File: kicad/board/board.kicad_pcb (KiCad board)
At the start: 2 copper layers, 110 x 70 mm, 72 parts, among them J0 Netz

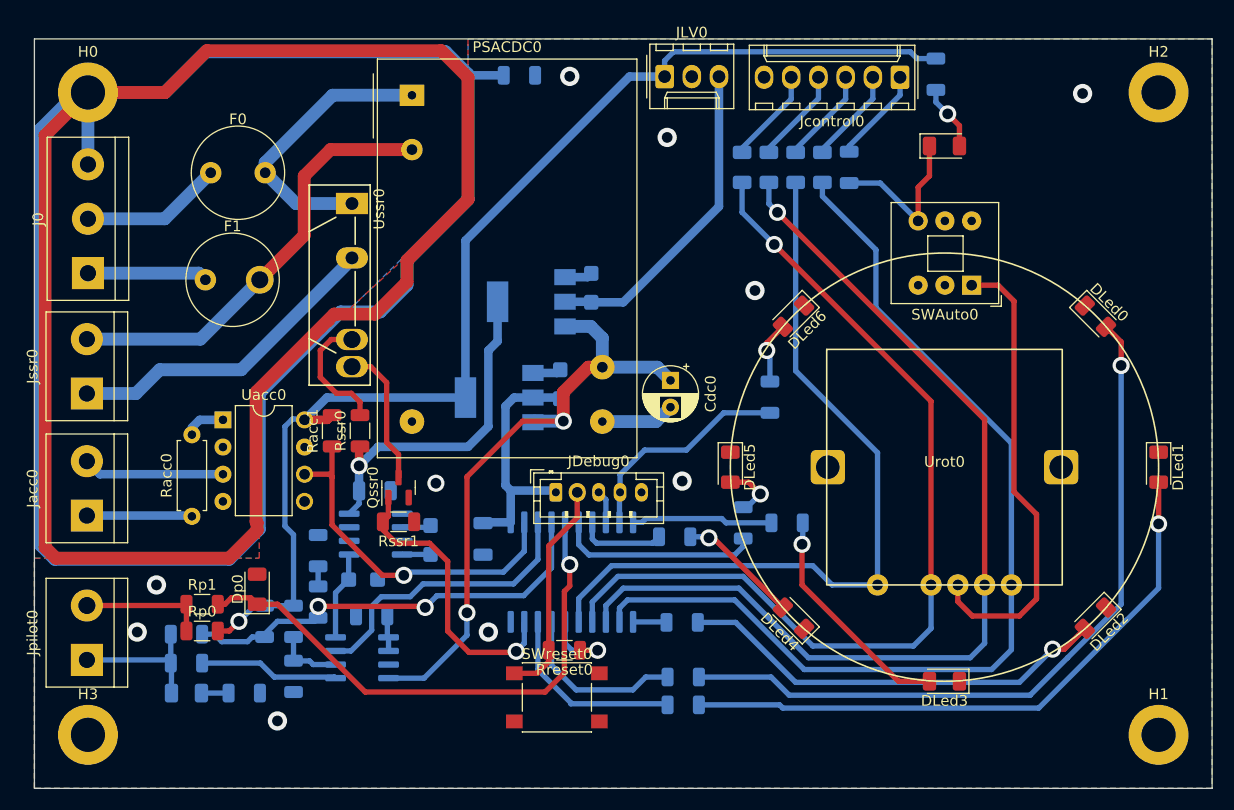
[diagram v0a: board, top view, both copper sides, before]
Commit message: hardware: kicad board bestellt
simplifiziert:
Strom sowie Fehlerstrom werden durch Hauptsicherung und FI gesichert.
AC-Check is a recht sinnlos weil gegen ein hängendes Relais kannst
eh nit viel tun.
Diodencheck macht sinn, wird auch mit -5V statt den Spezifizierten -12V
duchgeführt, sollt genauso funktionieren, meine LTC1044 halten max 9V aus.
Rechtck-Puls wird mit Transistor-Brücke realisiert (simuliert, nicht
getestet). Steigende Flanke wird begrenzt durch pull-down Widerstand
(auf -5V) und parasitic capazity.
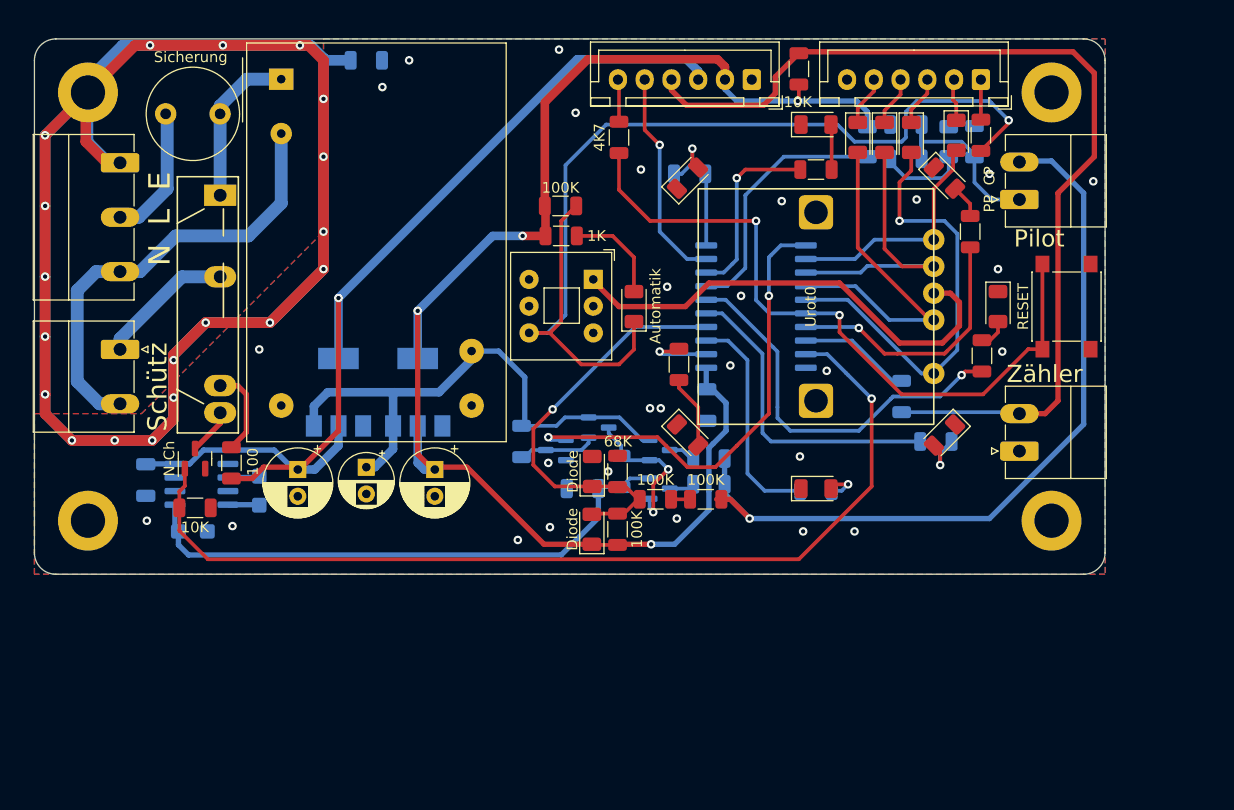
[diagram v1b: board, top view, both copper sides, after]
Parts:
- removed F1: 100m, Fuse:Fuse_Littelfuse_372_D8.50mm
- removed JDebug0: Conn_01x05, Connector_JST:JST_PH_B5B-PH-K_1x05_P2.00mm_Vertical
- removed JLV0: Conn_01x03, Connector_Molex:Molex_KK-254_AE-6410-03A_1x03_P2.54mm_Vertical
- removed Jacc0: AC-Control, TerminalBlock:TerminalBlock_bornier-2_P5.08mm
- removed Jpilot0: PILOT, TerminalBlock:TerminalBlock_bornier-2_P5.08mm
- removed Jssr0: Schütz, TerminalBlock:TerminalBlock_bornier-2_P5.08mm
- removed Racc0: 22K, Resistor_THT:R_Axial_DIN0207_L6.3mm_D2.5mm_P7.62mm_Horizontal
- removed Racc1, Rp1, Rpc0, Rpc8: 10K, Resistor_SMD:R_1206_3216Metric
- removed Rpc3: 1K, Resistor_SMD:R_1206_3216Metric
- removed Rpc6: 3K3, Resistor_SMD:R_1206_3216Metric
- removed Uacc0: MID400, Package_DIP:DIP-8_W7.62mm
- removed Upc0: LM358, Package_SO:SOIC-8_3.9x4.9mm_P1.27mm
- added (1K5): 1K5, Resistor_SMD:R_1206_3216Metric, B.Cu at (137.8, 59.6)
- added 100K: 100K, Resistor_SMD:R_1206_3216Metric, F.Cu at (99.1, 65.6)
- added 100K: 100K, Resistor_SMD:R_1206_3216Metric, F.Cu at (112.7, 93.0)
- added 10K: 10K, Resistor_SMD:R_1206_3216Metric, F.Cu at (121.4, 52.8)
- added 10K: 4K7, Resistor_SMD:R_1206_3216Metric, B.Cu at (131.4, 61.2)
- added 10K: 10k, Resistor_SMD:R_1206_3216Metric, B.Cu at (95.5, 87.6)
- added 10p: 10p, Capacitor_SMD:C_1206_3216Metric, B.Cu at (101.2, 92.0)
- added 1K: 1K, Resistor_SMD:R_1206_3216Metric, B.Cu at (113.0, 91.6)
- added 1K: 1K, Resistor_SMD:R_1206_3216Metric, B.Cu at (131.0, 83.4)
- added Diode: D, Diode_SMD:D_1206_3216Metric, F.Cu at (102.1, 95.8)
- added Diode: D, Diode_SMD:D_1206_3216Metric, B.Cu at (127.8, 59.6)
- added J1: Conn_01x02, Connector_Phoenix_MC:PhoenixContact_MC_1,5_2-G-3.5_1x02_P3.50mm_Horizontal, F.Cu at (142.0, 88.5)
- added J2: Schütz, Connector_Phoenix_MC_HighVoltage:PhoenixContact_MC_1,5_2-G-5.08_1x02_P5.08mm_Horizontal, F.Cu at (58.0, 79.0)
- added J3: Pilot, Connector_Phoenix_MC:PhoenixContact_MC_1,5_2-G-3.5_1x02_P3.50mm_Horizontal, F.Cu at (142.0, 65.0)
- added Jcontrol1: Conn_01x06, Connector_JST:JST_XH_B6B-XH-A_1x06_P2.50mm_Vertical, F.Cu at (117.0, 53.8)
- added N-Ch: MMBF170, Package_TO_SOT_SMD:SOT-23, B.Cu at (98.7, 88.4)
- added N-Ch: MMBF170, Package_TO_SOT_SMD:SOT-23, B.Cu at (108.4, 92.0)
- added P-Ch: IRLML5203, Package_TO_SOT_SMD:SOT-23, B.Cu at (108.4, 88.4)
- added P-Ch: IRLML5203, Package_TO_SOT_SMD:SOT-23, B.Cu at (102.7, 86.3)
- 100K: renamed from Rpc4; value 68K -> 100K; moved to F.Cu
- 100K: renamed from Rpc7; value 22K -> 100K; moved to F.Cu
- 1K: renamed from RAuto0; moved to F.Cu
- 3.3 V: renamed from Udc0
- 3K3: renamed from Rpc1; value 10K -> 3k3
- 3K3: renamed from Rp0; value 1K -> 3K3; moved to B.Cu
- 5 V: renamed from Udc1
- 68K: renamed from Rpc5; value 22K -> 68K; moved to F.Cu
- Cdc1, Cdc2: footprint Capacitor_Tantalum_SMD:CP_EIA-3216-12_Kemet-S -> Capacitor_THT:CP_Radial_D6.3mm_P2.50mm; moved to F.Cu
- Dc0, Dc1, Dc2, Dc3: moved to F.Cu
- Diode: renamed from Dpc0; moved to F.Cu
- Diode: renamed from Dp0; moved to B.Cu
- J0: footprint TerminalBlock:TerminalBlock_bornier-3_P5.08mm -> Connector_Phoenix_MC_HighVoltage:PhoenixContact_MC_1,5_3-G-5.08_1x03_P5.08mm_Horizontal
- Jcontrol0: footprint Connector_Molex:Molex_KK-254_AE-6410-06A_1x06_P2.54mm_Vertical -> Connector_JST:JST_XH_B6B-XH-A_1x06_P2.50mm_Vertical
- RAuto2: renamed from RAut1; moved to F.Cu
- RLed0, RLed4, RLed5: value 1K -> 470
- RLed1, RLed2, RLed3, RLed6: value 1K -> 470; moved to F.Cu
- moved 3K3 81.0 mm to (131.4, 58.0), turned to 180 degrees
- moved Diode 76.9 mm to (135.4, 59.6)
- moved RESET 60.0 mm to (146.4, 75.0), turned to 90 degrees
- moved 1K 52.4 mm to (113.0, 89.2)
- moved RLed1 51.5 mm to (123.0, 62.2)
- moved 4K7 48.2 mm to (104.6, 59.2), turned to 90 degrees
- moved RLed0 47.0 mm to (111.2, 62.6), turned to 180 degrees
- moved 100K 45.6 mm to (108.0, 93.0), turned to 0 degrees
- moved RLed2 45.3 mm to (137.4, 68.0), turned to 90 degrees
- moved DLed1 45.3 mm to (123.0, 58.0), turned to 0 degrees
- moved DLed2 43.5 mm to (135.0, 63.0), turned to -45 degrees
- moved Diode 43.2 mm to (102.1, 90.4), turned to 90 degrees
- moved DLed0 40.2 mm to (111.0, 63.0), turned to 45 degrees
- moved 1K 38.1 mm to (99.2, 68.4), turned to 180 degrees
- moved 3K3 36.1 mm to (104.8, 90.4)
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- renumbered Rgnd0 to 10, Rssr0 to 100, Rssr1 to 10K, Cndc0 to 10p, Cndc2 to 10u, Cndc1 to 10u, Rpc2 to 1K, Rreset0 to 4K7, Utiny0 to Attiny1616, Undc0 to LTC1044, DLed6 to Led6, Qssr0 to N-Ch, SWreset0 to RESET, F0 to Sicherung
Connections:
- 100K pad 2: Control Pilot -> Net-(Rpc4-Pad2)
- 1K pad 1: Net-(Upc0-Pad1) -> Control Pilot
- 1K pad 2: Control Pilot -> Net-(Q1-Pad3)
- 3K3 pad 2: GND -> -5V
- 68K pad 1: Net-(Rpc5-Pad1) -> GND
- Attiny1616 pad 10: Led3 -> Led0
- Attiny1616 pad 11: Led2 -> PWM
- Attiny1616 pad 17: Led0 -> Led2
- Attiny1616 pad 18: Led1 -> Stromzähler
- Attiny1616 pad 2: AC-Check -> Led6
- Attiny1616 pad 3: PWM -> Led5
- Attiny1616 pad 5: PP Read -> Led4
- Attiny1616 pad 6: Led5 -> Led3
- Attiny1616 pad 7: Led4 -> PP Read
- Attiny1616 pad 8: Uart_RX -> Led1
- Diode pad 1: Control Pilot -> CP-Read
- Diode pad 2: Net-(Rpc3-Pad2) -> GND
- J0 pad 1: /ACN -> Earth
- J0 pad 3: Earth -> VAC
- RESET pad 1: UPDI -> Net-(Rreset0-Pad1)
- RLed6 pad 1: Uart_TX -> Led6
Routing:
- net Zähler_ext: track 0.00 -> 92.1 mm
- net Auto: track 15.3 -> 96.5 mm, vias 0 -> 1
- net Earth: track 324.0 -> 246.0 mm, vias 0 -> 19
- net A: track 92.6 -> 21.9 mm
- net C: track 92.2 -> 26.5 mm, vias 1 -> 0
- net Net-(DLed0-Pad2): track 70.2 -> 5.46 mm
- net Relais: track 27.3 -> 90.7 mm
- net Control Pilot: track 13.5 -> 73.9 mm, vias 0 -> 1
- net Net-(Rreset0-Pad1): track 6.95 -> 65.9 mm, vias 1 -> 2
- net D: track 86.8 -> 32.1 mm, vias 1 -> 0
- net Net-(DLed1-Pad2): track 57.6 -> 4.23 mm, vias 1 -> 0
- net -5V: track 8.27 -> 52.8 mm
- net Net-(DLed2-Pad2): track 40.5 -> 3.13 mm, vias 1 -> 0
- net +5V: track 62.4 -> 97.1 mm
- net AC-Check: track 33.7 -> 0.00 mm, vias 1 -> 0
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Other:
- board size 110 x 70 mm -> 100 x 50 mm
- board text added: "+12V"
- board text added: "-5V"
- board text added: "Automatik"
- board text added: "Control Pilot"
- board text added: "E L N"
- board text added: "EVSE Wallbox Johnny Jan.2023"
- board text added: "N L E"
- board text added: "PP CP"
- board text added: "Pilot"
- board text added: "Prox. Pilot"
- board text added: "Relais"
- board text added: "Schütz"
- board text added: "UPDI TX Zähler 5V 3.3V GND"
- board text added: "X A B C D Gnd"
- board text added: "Zähler"

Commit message: hardware: korrekturen fehlerhaftes pcb
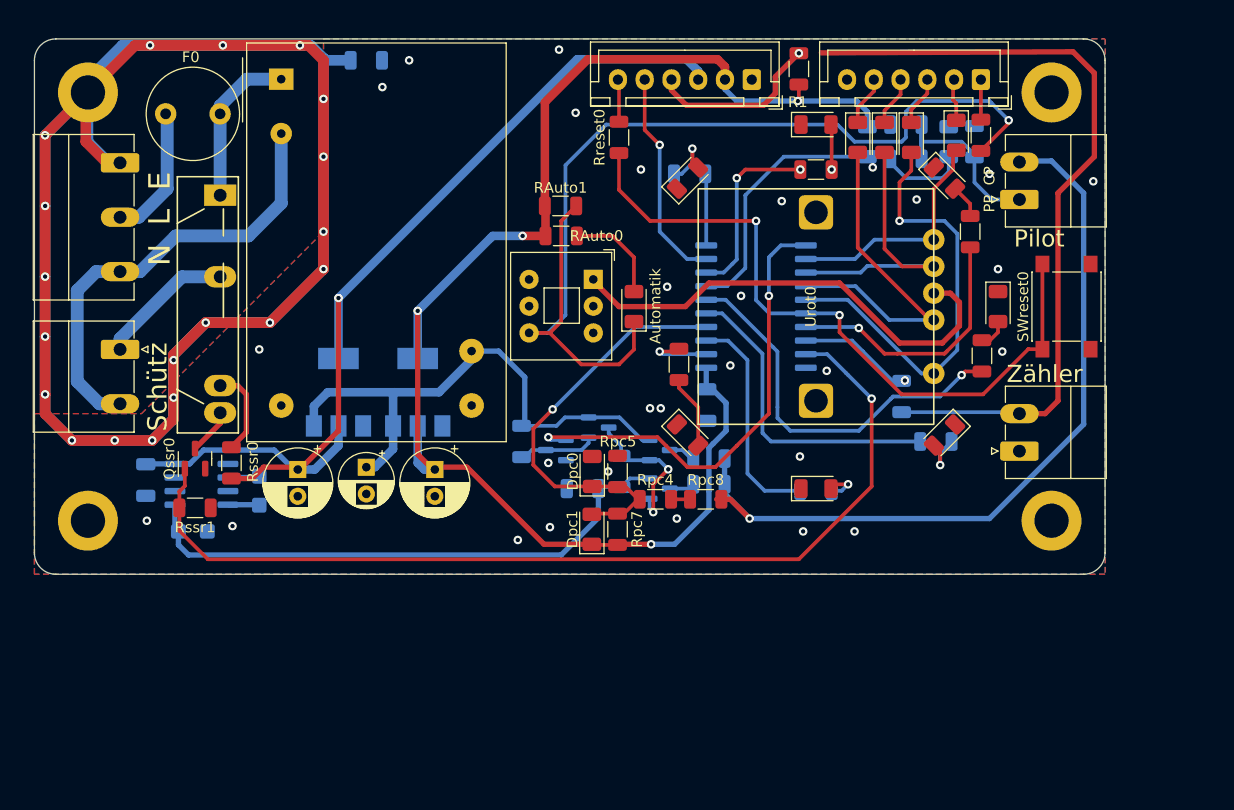
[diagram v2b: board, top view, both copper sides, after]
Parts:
- Udc0: renamed from 3.3 V
- Udc1: renamed from 5 V
- renumbered 10p to Cdpc1, 10p to Cndc0, 10u to Cndc1, 10u to Cndc2, Led6 to DLed6, Diode to Dp0, Diode to Dp1, Diode to Dpc0, Diode to Dpc1, Sicherung to F0, P-Ch to Q1, P-Ch to Q2, N-Ch to Qssr0, N-Ch to Qssr1, N-Ch to Qssr2, 10K to R1, 1K to R2, 1K to RAuto0, 100K to RAuto1, 10 to Rgnd0, 3K3 to Rp0, 10K to Rp1, 3K3 to Rpc1, 1K to Rpc2, 10K to Rpc3, 100K to Rpc4, 68K to Rpc5, 1K to Rpc6, 100K to Rpc7, 100K to Rpc8, (1K5) to Rpp0, 4K7 to Rreset0, 100 to Rssr0, 10K to Rssr1, RESET to SWreset0, LTC1044 to Undc0, Attiny1616 to Utiny0
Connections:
- DLed_auto0 pad 1: Auto -> PP Read
- J1 pad 2: Zähler_ext -> Net-(DLed1-Pad2)
- Jcontrol1 pad 4: Zähler_ext -> Uart_RX
- R1 pad 2: Zähler_ext -> Uart_RX
- R2 pad 1: Zähler_ext -> Net-(DLed1-Pad2)
- R2 pad 2: Stromzähler -> Led1
- RAuto1 pad 1: Auto -> PP Read
- RAuto2 pad 2: Auto -> PP Read
- RLed1 pad 1: Led1 -> Uart_RX
- Rp1 pad 1: PP Read -> Proximity Pilot
- Rp1 pad 2: Proximity Pilot -> unconnected-(Rp1-Pad2)
- SWAuto0 pad 1: Net-(SWAuto0-Pad1) -> GND
- SWAuto0 pad 6: Auto -> PP Read
- Urot0 pad 5: Net-(SWAuto0-Pad1) -> GND
- Utiny0 pad 18: Stromzähler -> Led1
- Utiny0 pad 8: Led1 -> Uart_RX
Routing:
- net PP Read: track 34.4 -> 176.9 mm, vias 0 -> 2
- net Net-(DLed1-Pad2): track 4.23 -> 113.7 mm, vias 0 -> 1
- net Auto: track 96.5 -> 0.00 mm, vias 1 -> 0
- net Zähler_ext: track 92.1 -> 0.00 mm
- net GND: track 0.00 -> 55.4 mm
- net Uart_RX: track 0.00 -> 46.3 mm, vias 0 -> 3
- net Net-(SWAuto0-Pad1): track 44.2 -> 0.00 mm
- net Stromzähler: track 10.5 -> 0.00 mm
- net Led1: track 17.2 -> 10.8 mm
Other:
- copper layers 2 -> 4
